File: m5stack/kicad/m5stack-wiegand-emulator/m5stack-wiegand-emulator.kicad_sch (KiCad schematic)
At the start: 42 parts, among them J1 2x15 socket header, J2 2x15 pin header, J3 1x5 female, T1 TestPoint, T2 TestPoint, T3 TestPoint, T4 TestPoint, U1 RP2040, U2 ISOW7841, U3 SN74LVC2G126-EP, U6 FISM 1769405241

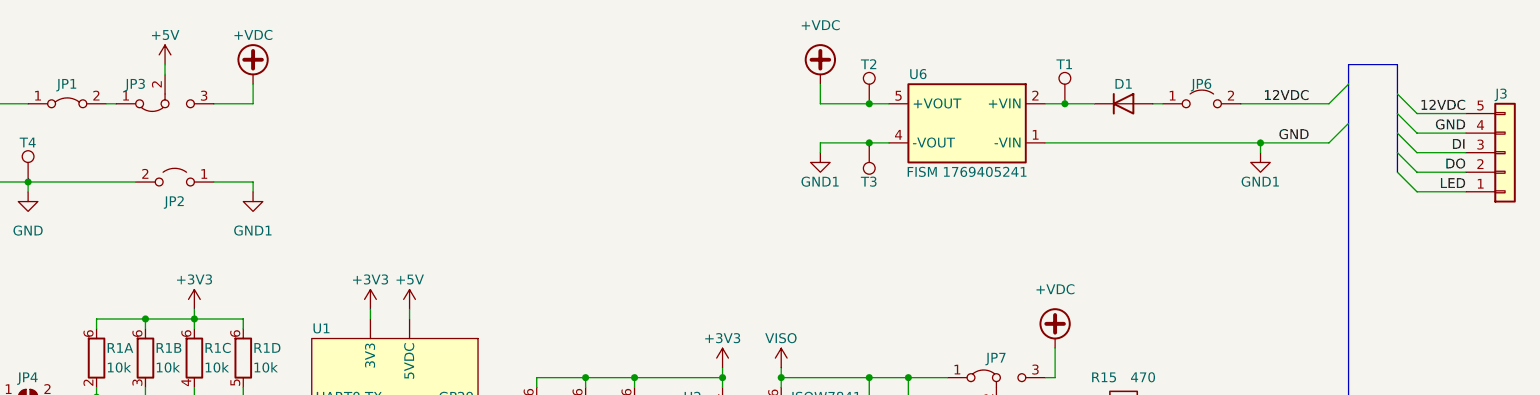
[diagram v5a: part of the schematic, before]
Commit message: Relocated J3 connector and rerouted
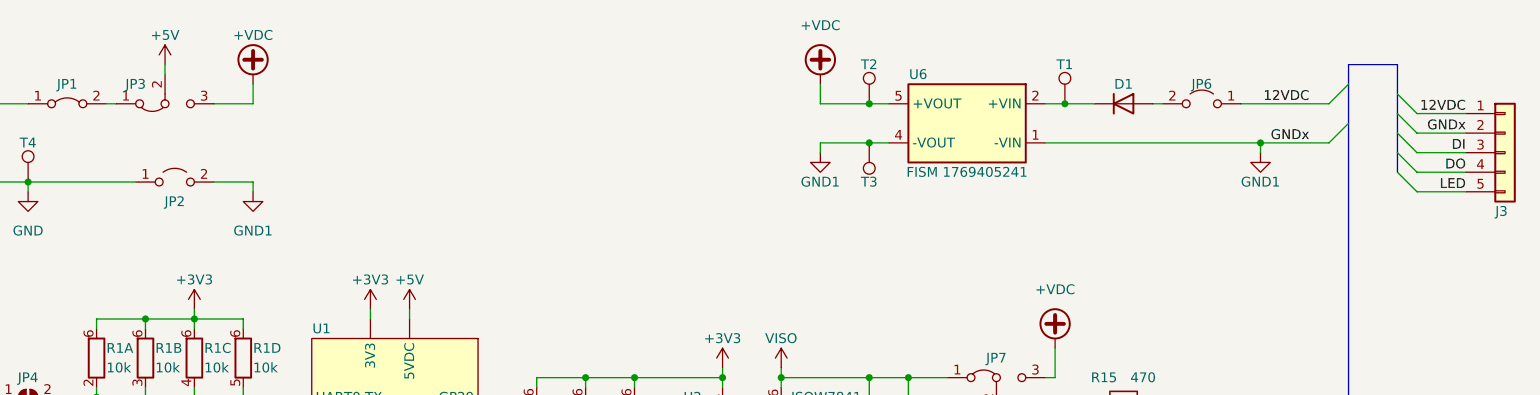
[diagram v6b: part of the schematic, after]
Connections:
- net 12VDC: now also J3.1 (Pin_1), JP6.1 (A); no longer J3.5 (Pin_5), JP6.2 (B)
- net DO: now also J3.4 (Pin_4); no longer J3.2 (Pin_2)
- net GND: no longer C1.2, C6.2, C7.2, D2.2 (A2), D3.2 (A2), D4.2 (A2), D5.1 (A), J3.4 (Pin_4), JP2.2 (B), LED1.3 (VSS), R8.2, T3.1, U2.15 (GND2), U2.9 (GND2), U3.4 (GND), U6.1 (-VIN), U6.4 (-VOUT)
- net LED: now also J3.5 (Pin_5); no longer J3.1 (Pin_1)
- net at D1.2 (A): now also JP6.2 (B); no longer JP6.1 (A)
- new net GND1: C1.2, C6.2, C7.2, D2.2 (A2), D3.2 (A2), D4.2 (A2), D5.1 (A), J3.2 (Pin_2), JP2.2 (B), LED1.3 (VSS), R8.2, T3.1, U2.15 (GND2), U2.9 (GND2), U3.4 (GND), U6.1 (-VIN), U6.4 (-VOUT)
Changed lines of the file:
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@@
     (effects (font (size 1.27 1.27)) (justify right bottom))
   )
-  (label "GND" (at 271.78 39.37 180) (fields_autoplaced)
+  (label "GNDx" (at 271.78 39.37 180) (fields_autoplaced)
     (effects (font (size 1.27 1.27)) (justify right bottom))
   )
@@
     (effects (font (size 1.27 1.27)) (justify right bottom))
   )
-  (label "GND" (at 251.46 40.64 180) (fields_autoplaced)
+  (label "GNDx" (at 251.46 40.64 180) (fields_autoplaced)
     (effects (font (size 1.27 1.27)) (justify right bottom))
   )
@@
     )
   )
-  (symbol (lib_id "uhppoted:Molex_PicoBlade_1x05") (at 276.86 41.91 0) (mirror x) (unit 1)
-    (in_bom yes) (on_board yes) (dnp no)
-    (property "Reference" "J3" (at 275.59 34.29 0)
-      (effects (font (size 1.27 1.27)) (justify left))
-    )
-    (property "Value" "1x5 female" (at 279.4 40.64 0)
+  (symbol (lib_id "uhppoted:Molex_PicoBlade_1x05") (at 276.86 41.91 0) (unit 1)
+    (in_bom yes) (on_board yes) (dnp no)
+    (property "Reference" "J3" (at 275.59 49.53 0)
+      (effects (font (size 1.27 1.27)) (justify left))
+    )
+    (property "Value" "1x5 female" (at 279.4 43.18 0)
       (effects (font (size 1.27 1.27)) (justify left) hide)
     )
@@
     )
   )
-  (symbol (lib_id "Jumper:Jumper_2_Open") (at 104.14 45.72 0) (mirror y) (unit 1)
+  (symbol (lib_id "Jumper:Jumper_2_Open") (at 104.14 45.72 0) (unit 1)
     (in_bom yes) (on_board yes) (dnp no)
     (property "Reference" "JP2" (at 104.14 48.26 0)
@@
     )
   )
-  (symbol (lib_id "Jumper:Jumper_2_Open") (at 237.49 35.56 0) (unit 1)
+  (symbol (lib_id "Jumper:Jumper_2_Open") (at 237.49 35.56 0) (mirror y) (unit 1)
     (in_bom yes) (on_board yes) (dnp no)
     (property "Reference" "JP6" (at 237.49 33.02 0)

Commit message: M5: fixed (most) ERC violations
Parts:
- JP8: renamed from JP6; value Jumper_2_Bridged -> Jumper
- renumbered JP8 to JP6, JP9 to JP7, JP7 to JP9
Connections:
- net 12VDC: now also JP8.2 (B); no longer JP8.1 (A)
- net at U1.9 (GP14), U2.4 (INB): now also R1.4 (R3.2); no longer R1.8 (R6.2)
- net at D1.2 (A): now also JP8.1 (A); no longer JP8.2 (B)
- net at U1.10 (GP13), U2.5 (INC): now also R1.3 (R2.2); no longer R1.9 (R7.2)
- net at JP6.2 (B), U1.19 (GP4): now also R1.8 (R6.2); no longer R1.4 (R3.2)
- net at U1.8 (GP15), U2.3 (INA): now also R1.5 (R4.2); no longer R1.7 (R5.2)
- net at JP7.2 (B), U1.18 (GP5): now also R1.7 (R5.2); no longer R1.5 (R4.2)
- net at JP5.2 (B), U1.22 (GP1): now also R1.9 (R7.2); no longer R1.3 (R2.2)
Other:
- moved on the sheet: C4, C6, C7, R1H

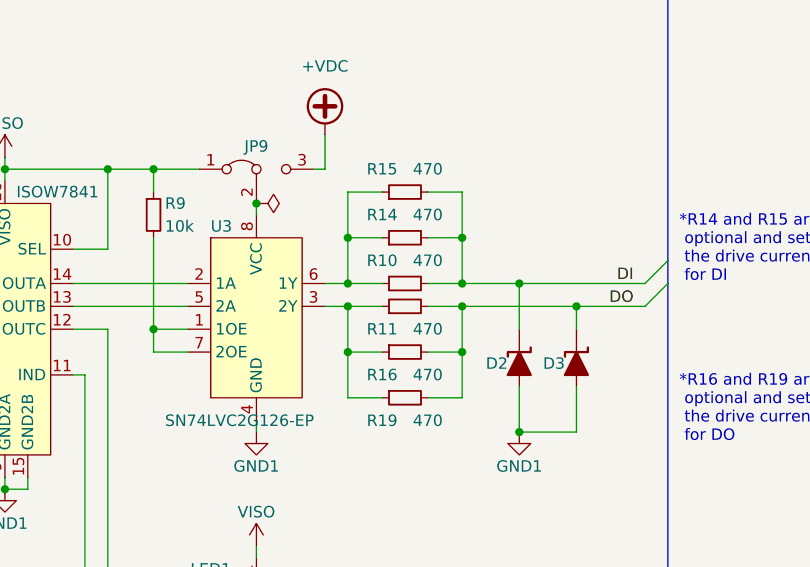
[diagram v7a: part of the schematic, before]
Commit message: M5: routed DI/DO signals
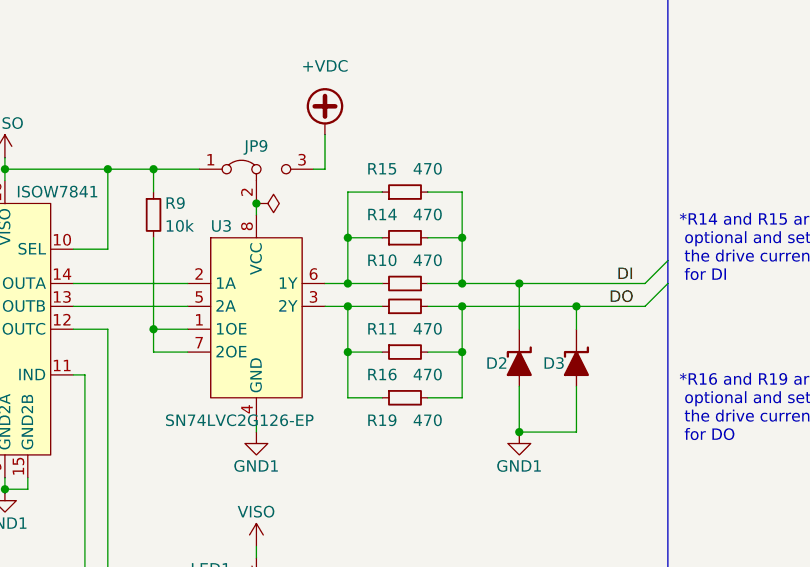
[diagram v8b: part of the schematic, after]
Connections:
- net DI: now also R10.1; no longer R10.2
- net at R14.1, R15.1, U3.6 (1Y): now also R10.2; no longer R10.1
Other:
- moved on the sheet: R10
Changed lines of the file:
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@@
     )
   )
-  (symbol (lib_id "Device:R_Small") (at 227.33 83.82 90) (unit 1)
+  (symbol (lib_id "Device:R_Small") (at 227.33 83.82 270) (mirror x) (unit 1)
     (in_bom yes) (on_board yes) (dnp no)
     (property "Reference" "R10" (at 224.79 81.28 90)
